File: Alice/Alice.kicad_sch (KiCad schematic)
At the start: 46 parts

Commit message: Copper DMA done
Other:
- sheet copper_dma ports: added COPRS, DRB[8..1], EUCP, UCB1, UCB2, UCI1, UCI2, UCP; removed none

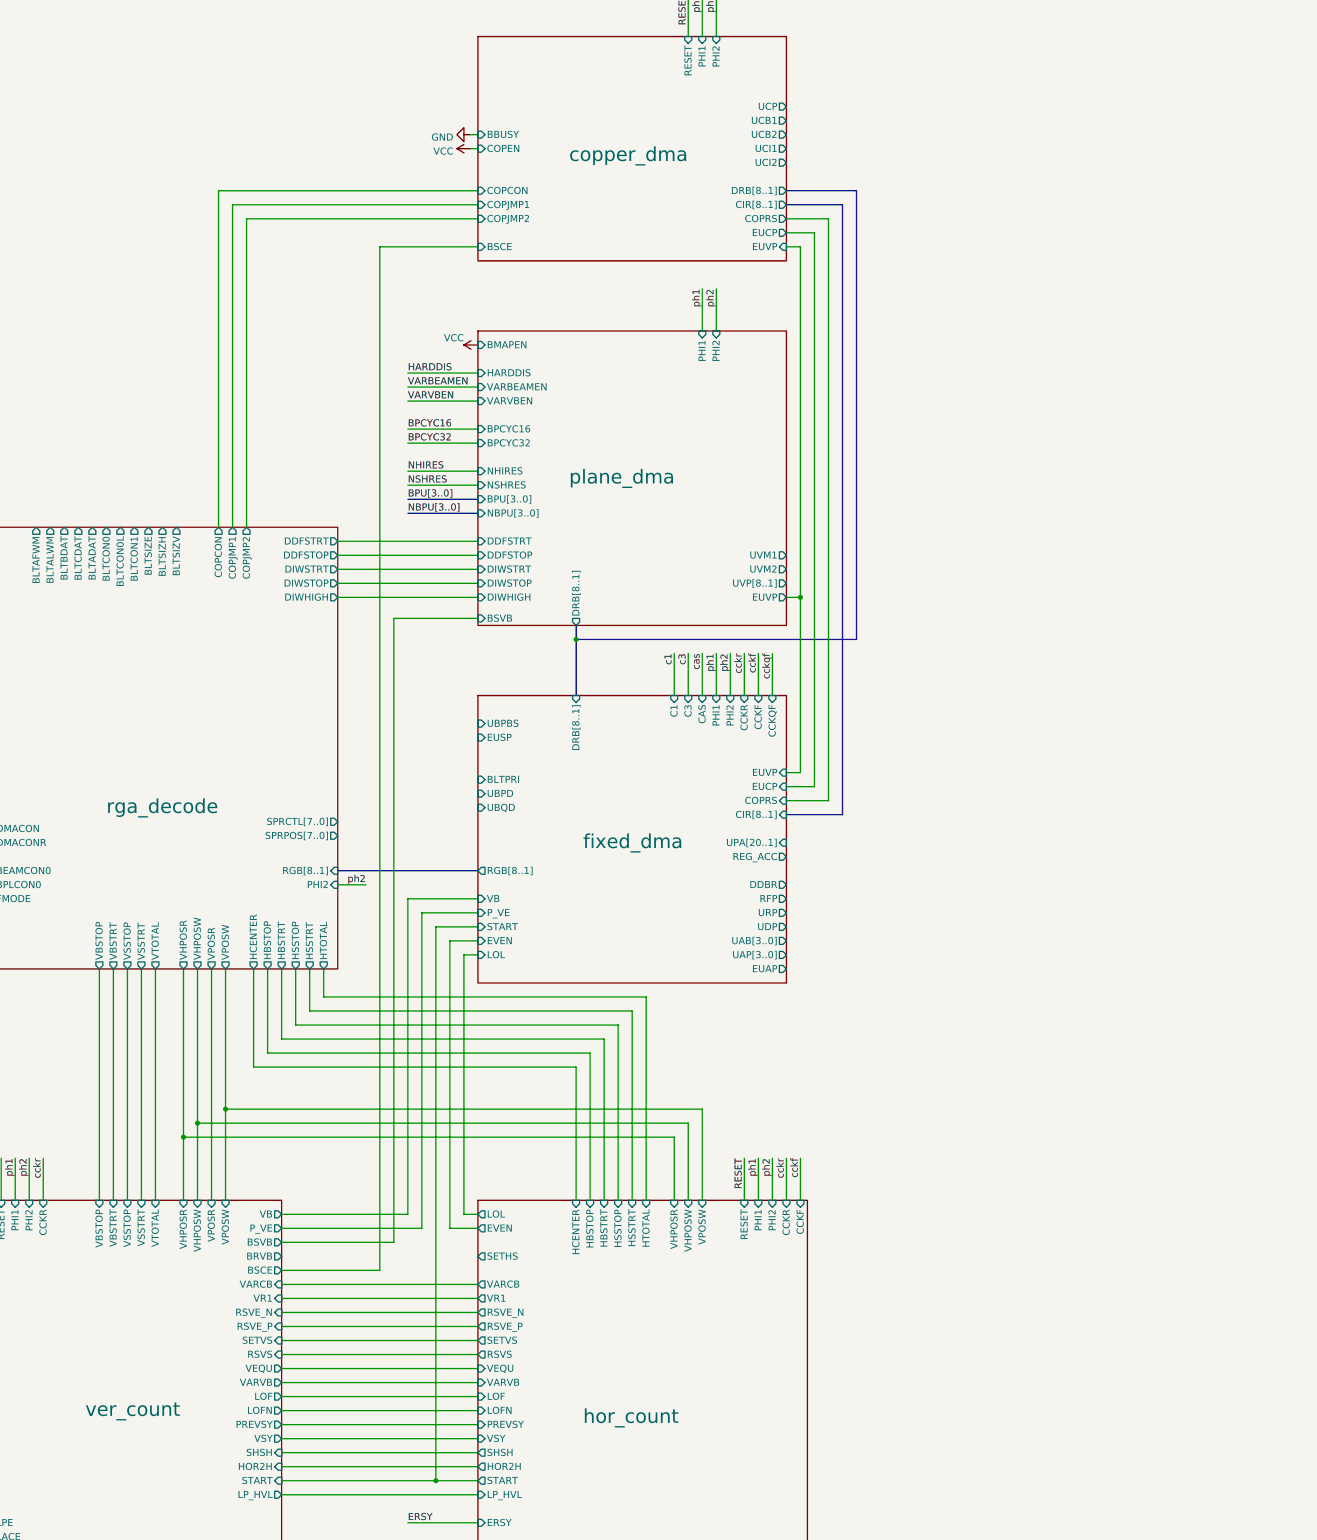
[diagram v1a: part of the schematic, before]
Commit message: Preparing DMA pointers sheet
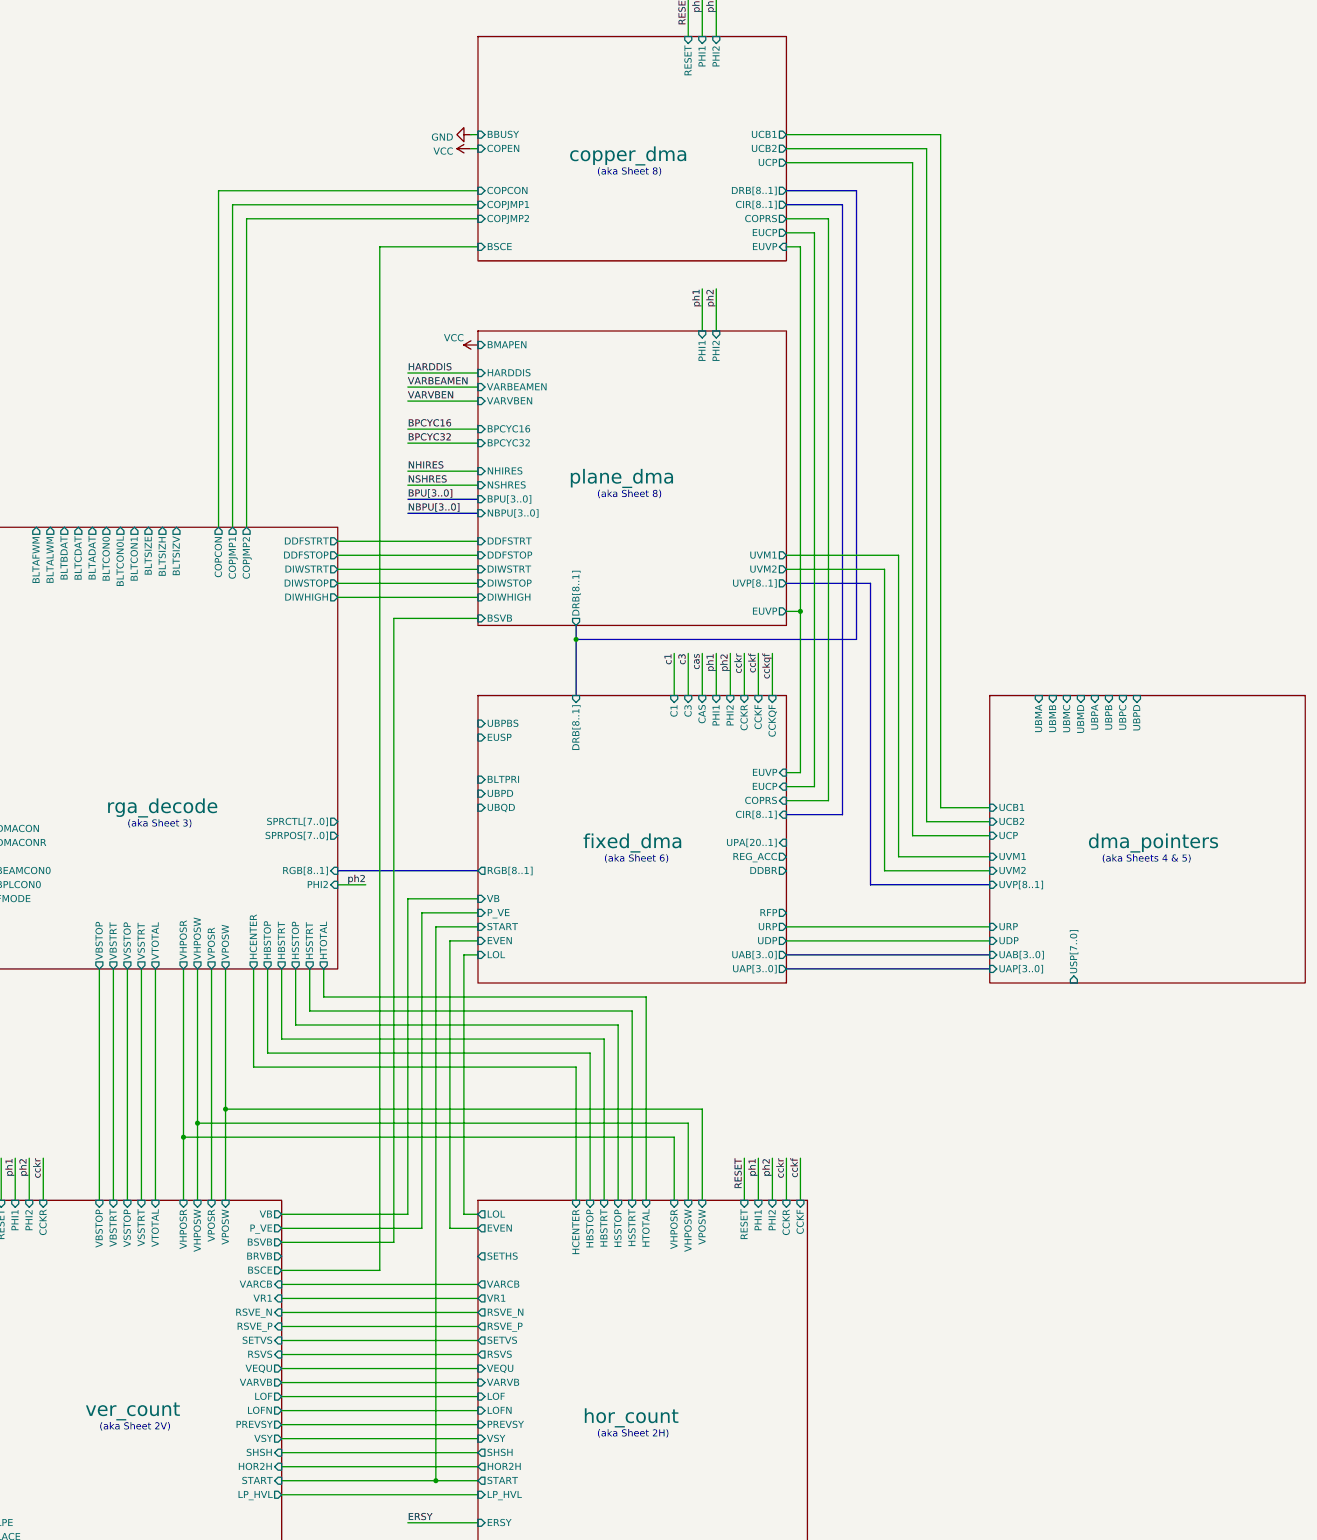
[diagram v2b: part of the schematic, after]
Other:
- added sheet dma_pointers (dma_pointers.kicad_sch)
- sheet copper_dma ports: added none; removed UCI1, UCI2
- sheet fixed_dma ports: added none; removed EUAP
- note added: "(aka Sheet 2H)"
- note added: "(aka Sheet 2V)"
- note added: "(aka Sheet 3)"
- note added: "(aka Sheet 6)"
- note added: "(aka Sheet 8)"
- note added: "(aka Sheets 4 & 5)"
